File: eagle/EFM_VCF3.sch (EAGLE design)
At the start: 42 parts, among them IC1 LM13700N, IC2 TL084P, Q3 2N3906, Q4 2N3906, U1 POWER

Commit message: started the board
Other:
- moved on the sheet: CUTOFF, IN1_LEV, IN_1, R21, R6
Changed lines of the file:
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@@
 <instance part="P+4" gate="1" x="106.68" y="60.452"/>
 <instance part="P-3" gate="1" x="106.68" y="14.224"/>
-<instance part="CUTOFF" gate="G$1" x="-45.72" y="55.88"/>
-<instance part="P+3" gate="1" x="-45.72" y="66.04"/>
-<instance part="R6" gate="G$1" x="-33.02" y="55.88" rot="R180"/>
+<instance part="CUTOFF" gate="G$1" x="-45.72" y="45.72"/>
+<instance part="P+3" gate="1" x="-45.72" y="55.88"/>
+<instance part="R6" gate="G$1" x="-33.02" y="45.72" rot="R180"/>
 <instance part="P+1" gate="1" x="132.08" y="57.912"/>
 <instance part="P-1" gate="1" x="132.08" y="21.844"/>
@@
 <instance part="R16" gate="G$1" x="132.08" y="124.46"/>
 <instance part="R17" gate="G$1" x="132.08" y="109.22"/>
-<instance part="P-7" gate="1" x="-45.72" y="45.72"/>
+<instance part="P-7" gate="1" x="-45.72" y="35.56"/>
 <instance part="IC2" gate="A" x="-53.34" y="99.06" rot="MR180"/>
 <instance part="IC2" gate="B" x="149.86" y="137.16"/>
@@
 <instance part="R18" gate="G$1" x="-17.78" y="71.12"/>
 <instance part="GND16" gate="1" x="-60.96" y="83.82"/>
-<instance part="IN_1" gate="G$1" x="-104.14" y="129.54" rot="MR180"/>
-<instance part="GND17" gate="1" x="-93.98" y="99.06"/>
+<instance part="IN_1" gate="G$1" x="-104.14" y="109.22" rot="MR180"/>
+<instance part="GND17" gate="1" x="-93.98" y="88.9"/>
 <instance part="R19" gate="G$1" x="-55.88" y="132.08"/>
 <instance part="R20" gate="G$1" x="-55.88" y="114.3"/>
-<instance part="IN1_LEV" gate="G$1" x="-88.9" y="129.54"/>
-<instance part="R21" gate="G$1" x="-78.74" y="129.54"/>
+<instance part="IN1_LEV" gate="G$1" x="-88.9" y="101.6"/>
+<instance part="R21" gate="G$1" x="-76.2" y="101.6"/>
 <instance part="R7" gate="G$1" x="88.9" y="81.28" rot="R270"/>
 <instance part="R22" gate="G$1" x="2.54" y="81.28" rot="R270"/>
@@
 <pinref part="GND17" gate="1" pin="GND"/>
 <pinref part="IN_1" gate="G$1" pin="RING"/>
-<wire x1="-93.98" y1="101.6" x2="-93.98" y2="124.46" width="0.1524" layer="91"/>
-<wire x1="-93.98" y1="124.46" x2="-93.98" y2="127" width="0.1524" layer="91"/>
-<wire x1="-93.98" y1="127" x2="-96.52" y2="127" width="0.1524" layer="91"/>
+<wire x1="-93.98" y1="91.44" x2="-93.98" y2="96.52" width="0.1524" layer="91"/>
+<wire x1="-93.98" y1="96.52" x2="-93.98" y2="106.68" width="0.1524" layer="91"/>
+<wire x1="-93.98" y1="106.68" x2="-96.52" y2="106.68" width="0.1524" layer="91"/>
 <pinref part="IN1_LEV" gate="G$1" pin="A"/>
-<wire x1="-88.9" y1="124.46" x2="-93.98" y2="124.46" width="0.1524" layer="91"/>
-<junction x="-93.98" y="124.46"/>
+<wire x1="-88.9" y1="96.52" x2="-93.98" y2="96.52" width="0.1524" layer="91"/>
+<junction x="-93.98" y="96.52"/>
 </segment>
 </net>
@@
 <pinref part="CUTOFF" gate="G$1" pin="E"/>
 <pinref part="P+3" gate="1" pin="+12V"/>
-<wire x1="-45.72" y1="60.96" x2="-45.72" y2="63.5" width="0.1524" layer="91"/>
+<wire x1="-45.72" y1="50.8" x2="-45.72" y2="53.34" width="0.1524" layer="91"/>
 </segment>
 <segment>
@@
 <segment>
 <pinref part="CUTOFF" gate="G$1" pin="A"/>
-<wire x1="-45.72" y1="50.8" x2="-45.72" y2="48.26" width="0.1524" layer="91"/>
+<wire x1="-45.72" y1="40.64" x2="-45.72" y2="38.1" width="0.1524" layer="91"/>
 <pinref part="P-7" gate="1" pin="-12V"/>
 </segment>
@@
 <pinref part="CUTOFF" gate="G$1" pin="S"/>
 <pinref part="R6" gate="G$1" pin="2"/>
-<wire x1="-38.1" y1="55.88" x2="-40.64" y2="55.88" width="0.1524" layer="91"/>
+<wire x1="-38.1" y1="45.72" x2="-40.64" y2="45.72" width="0.1524" layer="91"/>
 </segment>
 </net>
@@
 <segment>
 <pinref part="R6" gate="G$1" pin="1"/>
-<wire x1="-27.94" y1="55.88" x2="-25.4" y2="55.88" width="0.1524" layer="91"/>
+<wire x1="-27.94" y1="45.72" x2="-25.4" y2="45.72" width="0.1524" layer="91"/>
 <pinref part="R8" gate="G$1" pin="1"/>
 <wire x1="-25.4" y1="30.48" x2="-25.4" y2="15.24" width="0.1524" layer="91"/>
@@
 <junction x="-10.16" y="30.48"/>
 <pinref part="Q3" gate="G$1" pin="B"/>
-<wire x1="-27.94" y1="40.64" x2="-25.4" y2="40.64" width="0.1524" layer="91"/>
-<wire x1="-25.4" y1="30.48" x2="-25.4" y2="40.64" width="0.1524" layer="91"/>
 <junction x="-25.4" y="30.48"/>
-<wire x1="-25.4" y1="55.88" x2="-25.4" y2="40.64" width="0.1524" layer="91"/>
-<junction x="-25.4" y="40.64"/>
+<wire x1="-25.4" y1="45.72" x2="-25.4" y2="30.48" width="0.1524" layer="91"/>
 </segment>
 </net>
@@
 <pinref part="R18" gate="G$1" pin="2"/>
 <wire x1="-12.7" y1="71.12" x2="27.94" y2="71.12" width="0.1524" layer="91"/>
-</segment>
-</net>
-<net name="N$22" class="0">
-<segment>
-<pinref part="IN_1" gate="G$1" pin="TIP"/>
-<wire x1="-96.52" y1="134.62" x2="-88.9" y2="134.62" width="0.1524" layer="91"/>
-<pinref part="IN1_LEV" gate="G$1" pin="E"/>
 </segment>
 </net>
@@
 <pinref part="IN1_LEV" gate="G$1" pin="S"/>
 <pinref part="R21" gate="G$1" pin="1"/>
+<wire x1="-83.82" y1="101.6" x2="-81.28" y2="101.6" width="0.1524" layer="91"/>
 </segment>
 </net>
@@
 <segment>
 <pinref part="R21" gate="G$1" pin="2"/>
-<wire x1="-73.66" y1="129.54" x2="-73.66" y2="101.6" width="0.1524" layer="91"/>
+<wire x1="-71.12" y1="101.6" x2="-73.66" y2="101.6" width="0.1524" layer="91"/>
 <pinref part="R18" gate="G$1" pin="1"/>
 <wire x1="-22.86" y1="71.12" x2="-68.58" y2="71.12" width="0.1524" layer="91"/>
@@
 <wire x1="-60.96" y1="114.3" x2="-68.58" y2="114.3" width="0.1524" layer="91"/>
 <junction x="-68.58" y="114.3"/>
-<wire x1="-73.66" y1="101.6" x2="-68.58" y2="101.6" width="0.1524" layer="91"/>
+<wire x1="-71.12" y1="101.6" x2="-68.58" y2="101.6" width="0.1524" layer="91"/>
 </segment>
 </net>
@@
 </segment>
 </net>
+<net name="N$22" class="0">
+<segment>
+<pinref part="IN_1" gate="G$1" pin="TIP"/>
+<wire x1="-96.52" y1="114.3" x2="-88.9" y2="114.3" width="0.1524" layer="91"/>
+<pinref part="IN1_LEV" gate="G$1" pin="E"/>
+<wire x1="-88.9" y1="114.3" x2="-88.9" y2="106.68" width="0.1524" layer="91"/>
+</segment>
+</net>

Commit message: working on brd
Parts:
- added BP_GND, HP_GND: LSP10, solpad:LSP10
- BP_OUT, HP_OUT: value AUDIO-JACK -> LSP10; device erthenvar:AUDIO-JACK -> solpad:LSP10
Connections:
- net GND: now also BP_GND.MP, HP_GND.MP; no longer BP_OUT.RING, HP_OUT.RING
- net N$15: now also BP_OUT.MP; no longer BP_OUT.TIP
- net N$17: now also HP_OUT.MP; no longer HP_OUT.TIP
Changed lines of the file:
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@@
 <part name="P-8" library="supply1" deviceset="-12V" device=""/>
 <part name="LP_OUT" library="erthenvar" deviceset="AUDIO-JACK" device=""/>
-<part name="BP_OUT" library="erthenvar" deviceset="AUDIO-JACK" device=""/>
-<part name="HP_OUT" library="erthenvar" deviceset="AUDIO-JACK" device=""/>
 <part name="GND2" library="supply1" deviceset="GND" device=""/>
 <part name="CV_1" library="erthenvar" deviceset="AUDIO-JACK" device=""/>
@@
 <part name="R22" library="rcl" deviceset="R-US_" device="0207/7" value="10k"/>
 <part name="SCALE_TRIM" library="rcl" deviceset="R-TRIMM" device="64W" value="10k"/>
+<part name="HP_OUT" library="solpad" deviceset="LSP10" device=""/>
+<part name="HP_GND" library="solpad" deviceset="LSP10" device=""/>
+<part name="BP_OUT" library="solpad" deviceset="LSP10" device=""/>
+<part name="BP_GND" library="solpad" deviceset="LSP10" device=""/>
 </parts>
 <sheets>
@@
 <instance part="P-8" gate="1" x="93.98" y="24.384"/>
 <instance part="LP_OUT" gate="G$1" x="175.26" y="101.6" rot="R180"/>
-<instance part="BP_OUT" gate="G$1" x="175.26" y="116.84" rot="R180"/>
-<instance part="HP_OUT" gate="G$1" x="175.26" y="132.08" rot="R180"/>
 <instance part="GND2" gate="1" x="162.56" y="83.82"/>
 <instance part="CV_1" gate="G$1" x="-68.58" y="22.86" rot="MR180"/>
@@
 <instance part="R22" gate="G$1" x="2.54" y="81.28" rot="R270"/>
 <instance part="SCALE_TRIM" gate="G$1" x="22.86" y="10.16" rot="MR0"/>
+<instance part="HP_OUT" gate="1" x="170.18" y="137.16" rot="R270"/>
+<instance part="HP_GND" gate="1" x="170.18" y="129.54" rot="R270"/>
+<instance part="BP_OUT" gate="1" x="170.18" y="121.92" rot="R270"/>
+<instance part="BP_GND" gate="1" x="170.18" y="114.3" rot="R270"/>
 </instances>
 <busses>
@@
 <pinref part="GND2" gate="1" pin="GND"/>
 <wire x1="162.56" y1="86.36" x2="162.56" y2="99.06" width="0.1524" layer="91"/>
-<pinref part="HP_OUT" gate="G$1" pin="RING"/>
 <wire x1="162.56" y1="99.06" x2="162.56" y2="114.3" width="0.1524" layer="91"/>
 <wire x1="162.56" y1="114.3" x2="162.56" y2="129.54" width="0.1524" layer="91"/>
 <wire x1="162.56" y1="129.54" x2="167.64" y2="129.54" width="0.1524" layer="91"/>
-<pinref part="BP_OUT" gate="G$1" pin="RING"/>
 <wire x1="167.64" y1="114.3" x2="162.56" y2="114.3" width="0.1524" layer="91"/>
 <junction x="162.56" y="114.3"/>
@@
 <wire x1="167.64" y1="99.06" x2="162.56" y2="99.06" width="0.1524" layer="91"/>
 <junction x="162.56" y="99.06"/>
+<pinref part="HP_GND" gate="1" pin="MP"/>
+<pinref part="BP_GND" gate="1" pin="MP"/>
 </segment>
 <segment>
@@
 <segment>
 <pinref part="IC2" gate="C" pin="OUT"/>
-<pinref part="BP_OUT" gate="G$1" pin="TIP"/>
 <wire x1="167.64" y1="121.92" x2="160.02" y2="121.92" width="0.1524" layer="91"/>
 <pinref part="IC2" gate="C" pin="-IN"/>
@@
 <wire x1="160.02" y1="114.3" x2="160.02" y2="121.92" width="0.1524" layer="91"/>
 <junction x="160.02" y="121.92"/>
+<pinref part="BP_OUT" gate="1" pin="MP"/>
 </segment>
 </net>
@@
 <segment>
 <pinref part="IC2" gate="B" pin="OUT"/>
-<pinref part="HP_OUT" gate="G$1" pin="TIP"/>
 <wire x1="167.64" y1="137.16" x2="160.02" y2="137.16" width="0.1524" layer="91"/>
 <pinref part="IC2" gate="B" pin="-IN"/>
@@
 <wire x1="160.02" y1="129.54" x2="160.02" y2="137.16" width="0.1524" layer="91"/>
 <junction x="160.02" y="137.16"/>
-</segment>
-</net>
+<pinref part="HP_OUT" gate="1" pin="MP"/>
+</segment>
+</net>

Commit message: gcode
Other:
- moved on the sheet: R12
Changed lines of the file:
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@@
 <?xml version="1.0" encoding="utf-8"?>
 <!DOCTYPE eagle SYSTEM "eagle.dtd">
-<eagle version="7.2.0">
+<eagle version="7.1.0">
 <drawing>
 <settings>
@@
 <instance part="C1" gate="G$1" x="132.08" y="48.26"/>
 <instance part="C2" gate="G$1" x="132.08" y="33.02"/>
-<instance part="R12" gate="G$1" x="-10.16" y="20.32" rot="R270"/>
-<instance part="GND9" gate="1" x="-10.16" y="7.62"/>
+<instance part="R12" gate="G$1" x="-7.62" y="22.86" rot="R270"/>
+<instance part="GND9" gate="1" x="-7.62" y="12.7"/>
 <instance part="Q3" gate="G$1" x="0" y="30.48"/>
 <instance part="Q4" gate="G$1" x="10.16" y="30.48" rot="MR0"/>
@@
 <segment>
 <pinref part="R12" gate="G$1" pin="2"/>
-<wire x1="-10.16" y1="10.16" x2="-10.16" y2="15.24" width="0.1524" layer="91"/>
+<wire x1="-7.62" y1="15.24" x2="-7.62" y2="17.78" width="0.1524" layer="91"/>
 <pinref part="GND9" gate="1" pin="GND"/>
 </segment>
@@
 <wire x1="-25.4" y1="30.48" x2="-25.4" y2="15.24" width="0.1524" layer="91"/>
 <wire x1="-25.4" y1="15.24" x2="-27.94" y2="15.24" width="0.1524" layer="91"/>
-<wire x1="-2.54" y1="30.48" x2="-10.16" y2="30.48" width="0.1524" layer="91"/>
+<wire x1="-2.54" y1="30.48" x2="-7.62" y2="30.48" width="0.1524" layer="91"/>
 <pinref part="R11" gate="G$1" pin="1"/>
-<wire x1="-10.16" y1="30.48" x2="-25.4" y2="30.48" width="0.1524" layer="91"/>
+<wire x1="-7.62" y1="30.48" x2="-25.4" y2="30.48" width="0.1524" layer="91"/>
 <wire x1="-25.4" y1="10.16" x2="-25.4" y2="15.24" width="0.1524" layer="91"/>
 <junction x="-25.4" y="15.24"/>
 <pinref part="R12" gate="G$1" pin="1"/>
-<wire x1="-10.16" y1="25.4" x2="-10.16" y2="30.48" width="0.1524" layer="91"/>
-<junction x="-10.16" y="30.48"/>
+<wire x1="-7.62" y1="27.94" x2="-7.62" y2="30.48" width="0.1524" layer="91"/>
+<junction x="-7.62" y="30.48"/>
 <pinref part="Q3" gate="G$1" pin="B"/>
 <junction x="-25.4" y="30.48"/>

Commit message: fixed connections
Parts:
- R22: device rcl:R-US_0207/7 -> rcl:R-US_0309/10
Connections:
- removed net N$38: C1.+, CUTOFF.E, CUTOFF_INIT.E, R1.1, U1.+12V
- net +12V: now also C1.+, CUTOFF.E, CUTOFF_INIT.E, R1.1, U1.+12V
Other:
- moved on the sheet: C1, C2

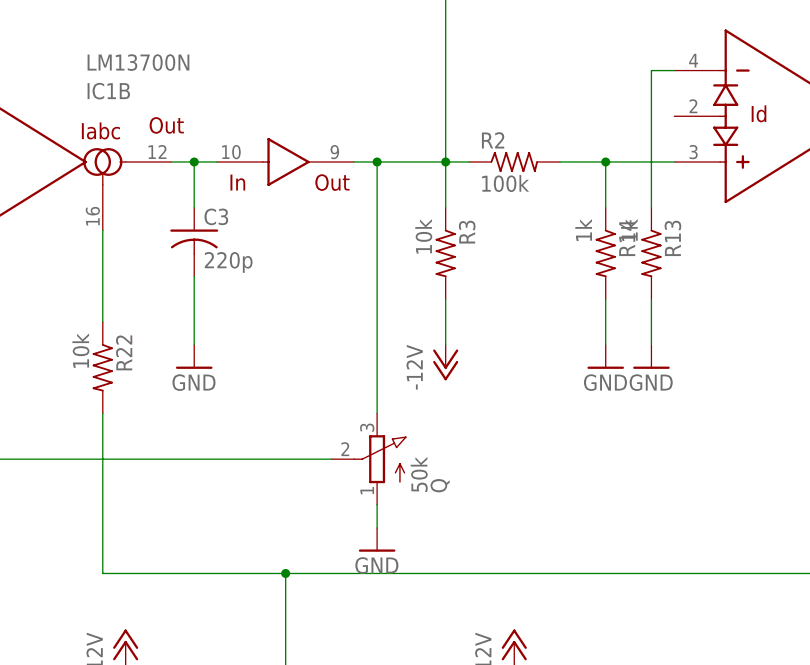
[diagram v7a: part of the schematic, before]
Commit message: fixed resonance direction
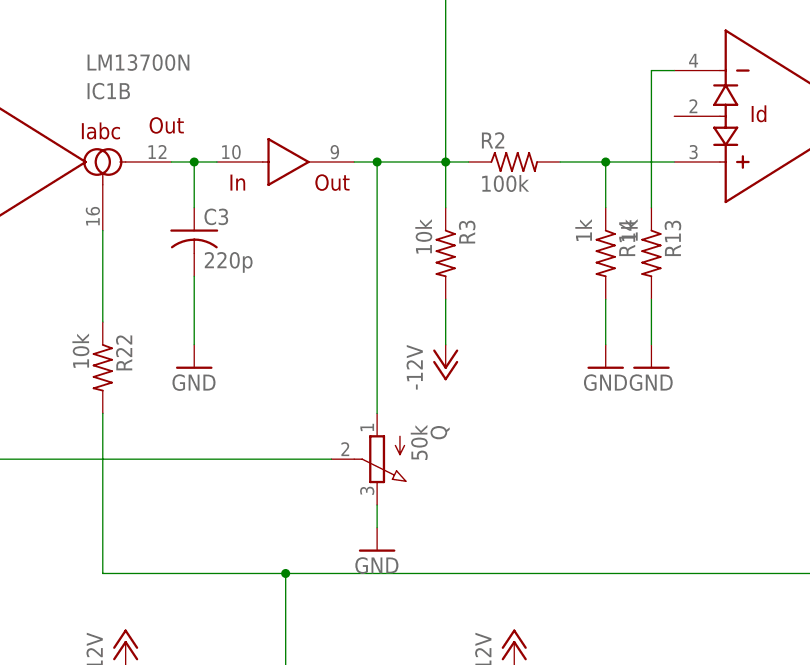
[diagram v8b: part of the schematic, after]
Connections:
- net GND: now also Q.E; no longer Q.A
- net N$5: now also Q.A; no longer Q.E
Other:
- moved on the sheet: Q
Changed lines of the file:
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@@
 <grid distance="0.1" unitdist="inch" unit="inch" style="lines" multiple="1" display="no" altdistance="0.01" altunitdist="inch" altunit="inch"/>
 <layers>
-<layer number="1" name="Top" color="4" fill="1" visible="yes" active="no"/>
-<layer number="16" name="Bottom" color="1" fill="1" visible="yes" active="no"/>
-<layer number="17" name="Pads" color="2" fill="1" visible="yes" active="no"/>
-<layer number="18" name="Vias" color="2" fill="1" visible="yes" active="no"/>
-<layer number="19" name="Unrouted" color="6" fill="1" visible="yes" active="no"/>
-<layer number="20" name="Dimension" color="15" fill="1" visible="yes" active="no"/>
-<layer number="21" name="tPlace" color="7" fill="1" visible="yes" active="no"/>
-<layer number="22" name="bPlace" color="7" fill="1" visible="yes" active="no"/>
-<layer number="23" name="tOrigins" color="15" fill="1" visible="yes" active="no"/>
-<layer number="24" name="bOrigins" color="15" fill="1" visible="yes" active="no"/>
-<layer number="25" name="tNames" color="7" fill="1" visible="yes" active="no"/>
-<layer number="26" name="bNames" color="7" fill="1" visible="yes" active="no"/>
-<layer number="27" name="tValues" color="7" fill="1" visible="yes" active="no"/>
-<layer number="28" name="bValues" color="7" fill="1" visible="yes" active="no"/>
+<layer number="1" name="Top" color="4" fill="1" visible="no" active="no"/>
+<layer number="16" name="Bottom" color="1" fill="1" visible="no" active="no"/>
+<layer number="17" name="Pads" color="2" fill="1" visible="no" active="no"/>
+<layer number="18" name="Vias" color="2" fill="1" visible="no" active="no"/>
+<layer number="19" name="Unrouted" color="6" fill="1" visible="no" active="no"/>
+<layer number="20" name="Dimension" color="15" fill="1" visible="no" active="no"/>
+<layer number="21" name="tPlace" color="7" fill="1" visible="no" active="no"/>
+<layer number="22" name="bPlace" color="7" fill="1" visible="no" active="no"/>
+<layer number="23" name="tOrigins" color="15" fill="1" visible="no" active="no"/>
+<layer number="24" name="bOrigins" color="15" fill="1" visible="no" active="no"/>
+<layer number="25" name="tNames" color="7" fill="1" visible="no" active="no"/>
+<layer number="26" name="bNames" color="7" fill="1" visible="no" active="no"/>
+<layer number="27" name="tValues" color="7" fill="1" visible="no" active="no"/>
+<layer number="28" name="bValues" color="7" fill="1" visible="no" active="no"/>
 <layer number="29" name="tStop" color="7" fill="3" visible="no" active="no"/>
 <layer number="30" name="bStop" color="7" fill="6" visible="no" active="no"/>
@@
 <layer number="35" name="tGlue" color="7" fill="4" visible="no" active="no"/>
 <layer number="36" name="bGlue" color="7" fill="5" visible="no" active="no"/>
-<layer number="37" name="tTest" color="7" fill="1" visible="yes" active="no"/>
-<layer number="38" name="bTest" color="7" fill="1" visible="yes" active="no"/>
+<layer number="37" name="tTest" color="7" fill="1" visible="no" active="no"/>
+<layer number="38" name="bTest" color="7" fill="1" visible="no" active="no"/>
 <layer number="39" name="tKeepout" color="4" fill="11" visible="no" active="no"/>
 <layer number="40" name="bKeepout" color="1" fill="11" visible="no" active="no"/>
@@
 <layer number="44" name="Drills" color="7" fill="1" visible="no" active="no"/>
 <layer number="45" name="Holes" color="7" fill="1" visible="no" active="no"/>
-<layer number="46" name="Milling" color="3" fill="1" visible="yes" active="no"/>
-<layer number="47" name="Measures" color="7" fill="1" visible="yes" active="no"/>
-<layer number="48" name="Document" color="7" fill="1" visible="yes" active="no"/>
-<layer number="49" name="Reference" color="7" fill="1" visible="yes" active="no"/>
-<layer number="50" name="dxf" color="7" fill="1" visible="yes" active="no"/>
-<layer number="51" name="tDocu" color="7" fill="1" visible="yes" active="no"/>
-<layer number="52" name="bDocu" color="7" fill="1" visible="yes" active="no"/>
-<layer number="53" name="tGND_GNDA" color="7" fill="9" visible="yes" active="no"/>
-<layer number="54" name="bGND_GNDA" color="1" fill="9" visible="yes" active="no"/>
-<layer number="56" name="wert" color="7" fill="1" visible="yes" active="no"/>
+<layer number="46" name="Milling" color="3" fill="1" visible="no" active="no"/>
+<layer number="47" name="Measures" color="7" fill="1" visible="no" active="no"/>
+<layer number="48" name="Document" color="7" fill="1" visible="no" active="no"/>
+<layer number="49" name="Reference" color="7" fill="1" visible="no" active="no"/>
+<layer number="50" name="dxf" color="7" fill="1" visible="no" active="no"/>
+<layer number="51" name="tDocu" color="7" fill="1" visible="no" active="no"/>
+<layer number="52" name="bDocu" color="7" fill="1" visible="no" active="no"/>
+<layer number="53" name="tGND_GNDA" color="7" fill="9" visible="no" active="no"/>
+<layer number="54" name="bGND_GNDA" color="1" fill="9" visible="no" active="no"/>
+<layer number="56" name="wert" color="7" fill="1" visible="no" active="no"/>
 <layer number="90" name="Modules" color="5" fill="1" visible="yes" active="yes"/>
 <layer number="91" name="Nets" color="2" fill="1" visible="yes" active="yes"/>
@@
 <instance part="CV_1" gate="G$1" x="-68.58" y="22.86" rot="MR180"/>
 <instance part="GND13" gate="1" x="-58.42" y="5.08"/>
-<instance part="Q" gate="G$1" x="33.02" y="71.12" rot="MR0"/>
+<instance part="Q" gate="G$1" x="33.02" y="71.12" rot="R180"/>
 <instance part="GND15" gate="1" x="33.02" y="60.96"/>
 <instance part="R18" gate="G$1" x="-17.78" y="71.12"/>
@@
 </segment>
 <segment>
-<pinref part="Q" gate="G$1" pin="A"/>
-<pinref part="GND15" gate="1" pin="GND"/>
-<wire x1="33.02" y1="63.5" x2="33.02" y2="66.04" width="0.1524" layer="91"/>
-</segment>
-<segment>
 <pinref part="IC2" gate="A" pin="+IN"/>
 <pinref part="GND16" gate="1" pin="GND"/>
@@
 <junction x="-93.98" y="96.52"/>
 </segment>
+<segment>
+<pinref part="Q" gate="G$1" pin="E"/>
+<pinref part="GND15" gate="1" pin="GND"/>
+<wire x1="33.02" y1="63.5" x2="33.02" y2="66.04" width="0.1524" layer="91"/>
+</segment>
 </net>
 <net name="N$10" class="0">
@@
 <wire x1="40.64" y1="99.06" x2="40.64" y2="104.14" width="0.1524" layer="91"/>
 <junction x="40.64" y="104.14"/>
-<pinref part="Q" gate="G$1" pin="E"/>
-<wire x1="33.02" y1="76.2" x2="33.02" y2="104.14" width="0.1524" layer="91"/>
-<junction x="33.02" y="104.14"/>
 <pinref part="R16" gate="G$1" pin="1"/>
 <wire x1="127" y1="124.46" x2="40.64" y2="124.46" width="0.1524" layer="91"/>
 <wire x1="40.64" y1="124.46" x2="40.64" y2="104.14" width="0.1524" layer="91"/>
-</segment>
-</net>
+<wire x1="33.02" y1="104.14" x2="33.02" y2="76.2" width="0.1524" layer="91"/>
+<junction x="33.02" y="104.14"/>
+<pinref part="Q" gate="G$1" pin="A"/>
+</segment>
+</net>
